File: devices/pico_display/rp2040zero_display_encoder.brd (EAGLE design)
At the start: 57.3 x 19.4 mm, 16 parts, among them U1 RP2040-ZERO', U2 EC12E20-24P24C-SW

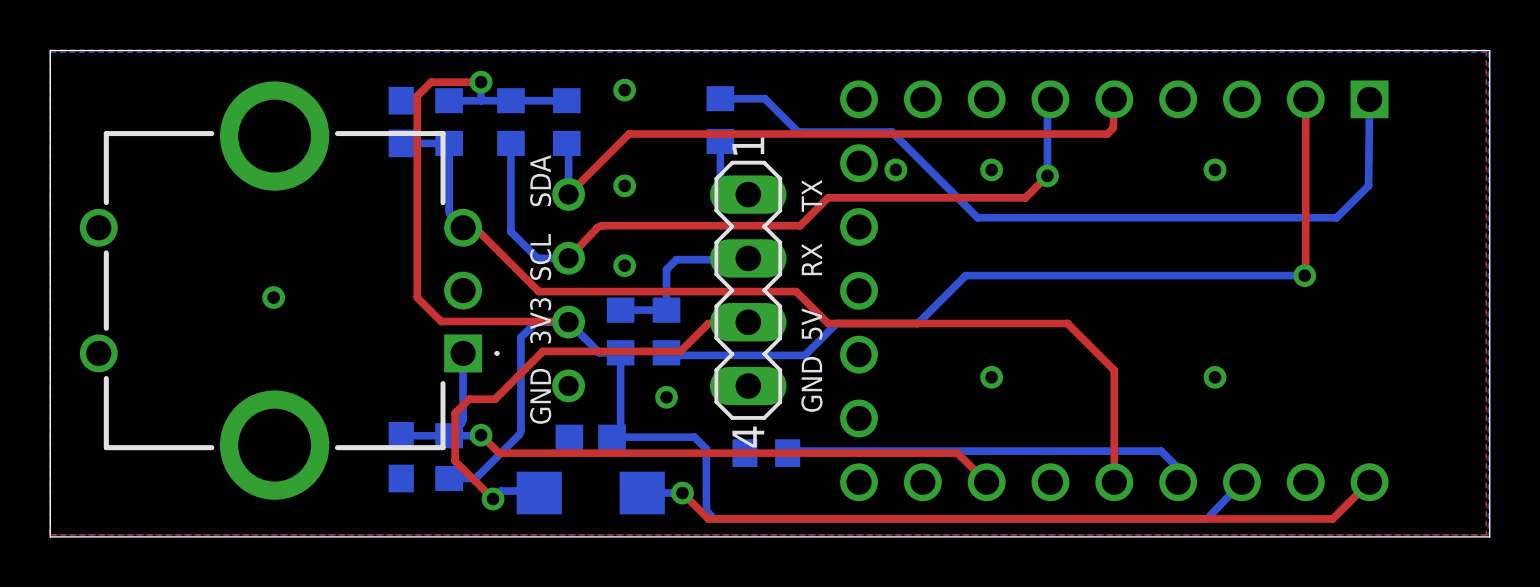
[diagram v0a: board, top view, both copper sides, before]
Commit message: fixes to display sch and brd
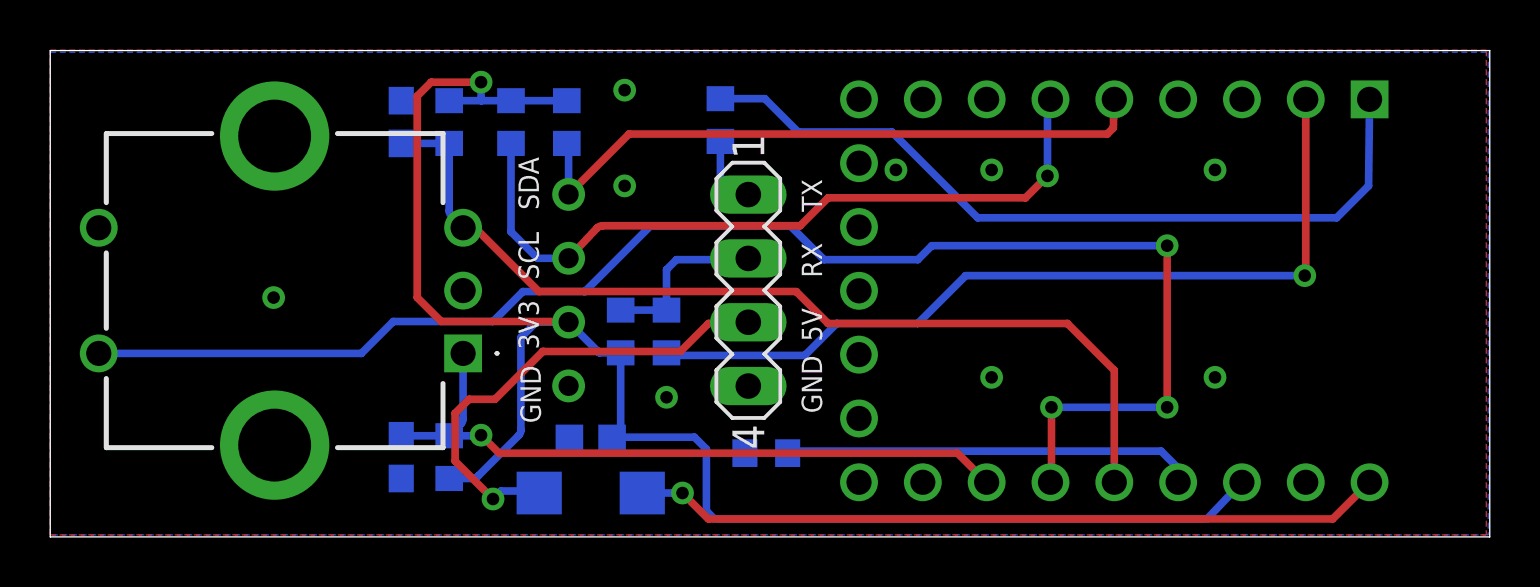
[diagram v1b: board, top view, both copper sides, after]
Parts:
- C1: value (none) -> 100nF
- R3: value 0R -> 1k
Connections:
- net BTN_ENTER_ENC_PUSH: now also U2.S1
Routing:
- net BTN_ENTER_ENC_PUSH: track 0.00 -> 59.4 mm, vias 0 -> 3
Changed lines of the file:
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@@
 <layer number="14" name="Route14" color="1" fill="6" visible="no" active="no"/>
 <layer number="15" name="Route15" color="4" fill="6" visible="no" active="no"/>
-<layer number="16" name="Bottom" color="1" fill="1" visible="no" active="yes"/>
+<layer number="16" name="Bottom" color="1" fill="1" visible="yes" active="yes"/>
 <layer number="17" name="Pads" color="2" fill="1" visible="yes" active="yes"/>
 <layer number="18" name="Vias" color="2" fill="1" visible="yes" active="yes"/>
 <layer number="19" name="Unrouted" color="6" fill="1" visible="yes" active="yes"/>
 <layer number="20" name="Dimension" color="15" fill="1" visible="yes" active="yes"/>
-<layer number="21" name="tPlace" color="7" fill="1" visible="yes" active="yes"/>
+<layer number="21" name="tPlace" color="7" fill="1" visible="no" active="yes"/>
 <layer number="22" name="bPlace" color="7" fill="1" visible="no" active="yes"/>
-<layer number="23" name="tOrigins" color="15" fill="1" visible="yes" active="yes"/>
+<layer number="23" name="tOrigins" color="15" fill="1" visible="no" active="yes"/>
 <layer number="24" name="bOrigins" color="15" fill="1" visible="no" active="yes"/>
 <layer number="25" name="tNames" color="7" fill="1" visible="no" active="yes"/>
@@
 <layer number="49" name="Reference" color="7" fill="1" visible="no" active="yes"/>
 <layer number="50" name="dxf" color="7" fill="1" visible="no" active="no"/>
-<layer number="51" name="tDocu" color="7" fill="1" visible="yes" active="yes"/>
+<layer number="51" name="tDocu" color="7" fill="1" visible="no" active="yes"/>
 <layer number="52" name="bDocu" color="7" fill="1" visible="no" active="yes"/>
 <layer number="53" name="tGND_GNDA" color="7" fill="9" visible="no" active="no"/>
@@
 <wire x1="38.23875" y1="23.8" x2="-19.05" y2="23.8" width="0" layer="20"/>
 <wire x1="-19.05" y1="23.8" x2="-19.05" y2="4.445" width="0" layer="20"/>
-<text x="0.873125" y="17.541875" size="0.8128" layer="25" font="vector" ratio="20" rot="R90">SDA</text>
-<text x="0.873125" y="14.605" size="0.8128" layer="25" font="vector" ratio="20" rot="R90">SCL</text>
-<text x="0.873125" y="8.89" size="0.8128" layer="25" font="vector" ratio="20" rot="R90">GND</text>
+<text x="0.396875" y="17.4625" size="0.8128" layer="25" font="vector" ratio="20" rot="R90">SDA</text>
+<text x="0.396875" y="14.684375" size="0.8128" layer="25" font="vector" ratio="20" rot="R90">SCL</text>
+<text x="0.47625" y="8.969375" size="0.8128" layer="25" font="vector" ratio="20" rot="R90">GND</text>
 <text x="6.270625" y="9.286875" size="0.8128" layer="26" font="vector" ratio="20" rot="MR90">GND</text>
 <text x="6.270625" y="12.303125" size="0.8128" layer="26" font="vector" ratio="20" rot="MR90">5V</text>
@@
 <text x="11.668125" y="9.36625" size="0.8128" layer="25" font="vector" ratio="20" rot="R90">GND</text>
 <text x="11.668125" y="12.22375" size="0.8128" layer="25" font="vector" ratio="20" rot="R90">5V</text>
-<text x="0.873125" y="12.065" size="0.8128" layer="25" font="vector" ratio="20" rot="R90">3V3</text>
+<text x="0.396875" y="11.90625" size="0.8128" layer="25" font="vector" ratio="20" rot="R90">3V3</text>
 <rectangle x1="1.508125" y1="5.318125" x2="3.33375" y2="7.064375" layer="42"/>
 <text x="-6.111875" y="14.76375" size="1.016" layer="26" font="vector" ratio="20" rot="MR0">CE display</text>
@@
 <element name="R2" library="resistor" package="R0603" value="1k" x="5.476875" y="12.620625" smashed="yes" rot="MR270"/>
 <element name="D1" library="diode" package="DO214AC" value="SK110-DIO" x="2.460625" y="6.19125" smashed="yes" rot="MR0"/>
-<element name="R3" library="resistor" package="R0603" value="0R" x="9.445625" y="7.77875" smashed="yes" rot="MR180"/>
+<element name="R3" library="resistor" package="R0603" value="1k" x="9.445625" y="7.77875" smashed="yes" rot="MR180"/>
 <element name="U$1" library="OLED" package="SIP" value="OLED" x="19.129375" y="14.614375" smashed="yes"/>
-<element name="C1" library="rcl" package="C0603" value="" x="2.460625" y="8.41375" smashed="yes" rot="MR0">
+<element name="C1" library="rcl" package="C0603" value="100nF" x="2.460625" y="8.41375" smashed="yes" rot="MR0">
 <attribute name="VALUE" x="3.095625" y="6.50875" size="1.27" layer="28" rot="MR0"/>
 </element>
@@
 <via x="5.476875" y="10.00125" extent="1-16" drill="0.5"/>
 <via x="-10.16" y="13.97" extent="1-16" drill="0.5"/>
-<via x="3.81" y="15.24" extent="1-16" drill="0.5"/>
 <via x="3.81" y="22.225" extent="1-16" drill="0.5"/>
 <via x="18.415" y="19.05" extent="1-16" drill="0.5"/>
@@
 <signal name="BTN_ENTER_ENC_PUSH">
 <contactref element="U1" pad="18"/>
+<contactref element="U2" pad="S1"/>
+<wire x1="-17.119375" y1="11.7475" x2="-6.6675" y2="11.7475" width="0.3048" layer="16"/>
+<wire x1="-6.6675" y1="11.7475" x2="-5.3975" y2="13.0175" width="0.3048" layer="16"/>
+<wire x1="-5.3975" y1="13.0175" x2="-1.42875" y2="13.0175" width="0.3048" layer="16"/>
+<wire x1="-1.42875" y1="13.0175" x2="-0.238125" y2="14.208125" width="0.3048" layer="16"/>
+<wire x1="-0.238125" y1="14.208125" x2="2.2225" y2="14.208125" width="0.3048" layer="16"/>
+<wire x1="2.2225" y1="14.208125" x2="4.841875" y2="16.8275" width="0.3048" layer="16"/>
+<wire x1="4.841875" y1="16.8275" x2="10.398125" y2="16.8275" width="0.3048" layer="16"/>
+<wire x1="10.398125" y1="16.8275" x2="11.7475" y2="15.478125" width="0.3048" layer="16"/>
+<via x="25.4" y="16.03375" extent="1-16" drill="0.5"/>
+<wire x1="25.4" y1="16.03375" x2="25.4" y2="9.604375" width="0.3048" layer="1"/>
+<via x="25.4" y="9.604375" extent="1-16" drill="0.5"/>
+<wire x1="25.4" y1="9.604375" x2="20.79625" y2="9.604375" width="0.3048" layer="16"/>
+<via x="20.79625" y="9.604375" extent="1-16" drill="0.5"/>
+<wire x1="20.79625" y1="9.604375" x2="20.79625" y2="6.658125" width="0.3048" layer="1"/>
+<wire x1="20.79625" y1="6.658125" x2="20.756875" y2="6.61875" width="0.3048" layer="1"/>
+<wire x1="11.7475" y1="15.478125" x2="15.478125" y2="15.478125" width="0.3048" layer="16"/>
+<wire x1="15.478125" y1="15.478125" x2="16.03375" y2="16.03375" width="0.3048" layer="16"/>
+<wire x1="16.03375" y1="16.03375" x2="25.4" y2="16.03375" width="0.3048" layer="16"/>
 </signal>
 <signal name="BTN_RIGHT_ENC_B">
